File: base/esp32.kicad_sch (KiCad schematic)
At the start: 7 parts, among them SW1 SW_Push_Open, SW2 SW_Push_Open, U2 ESP32-S3-WROOM-2

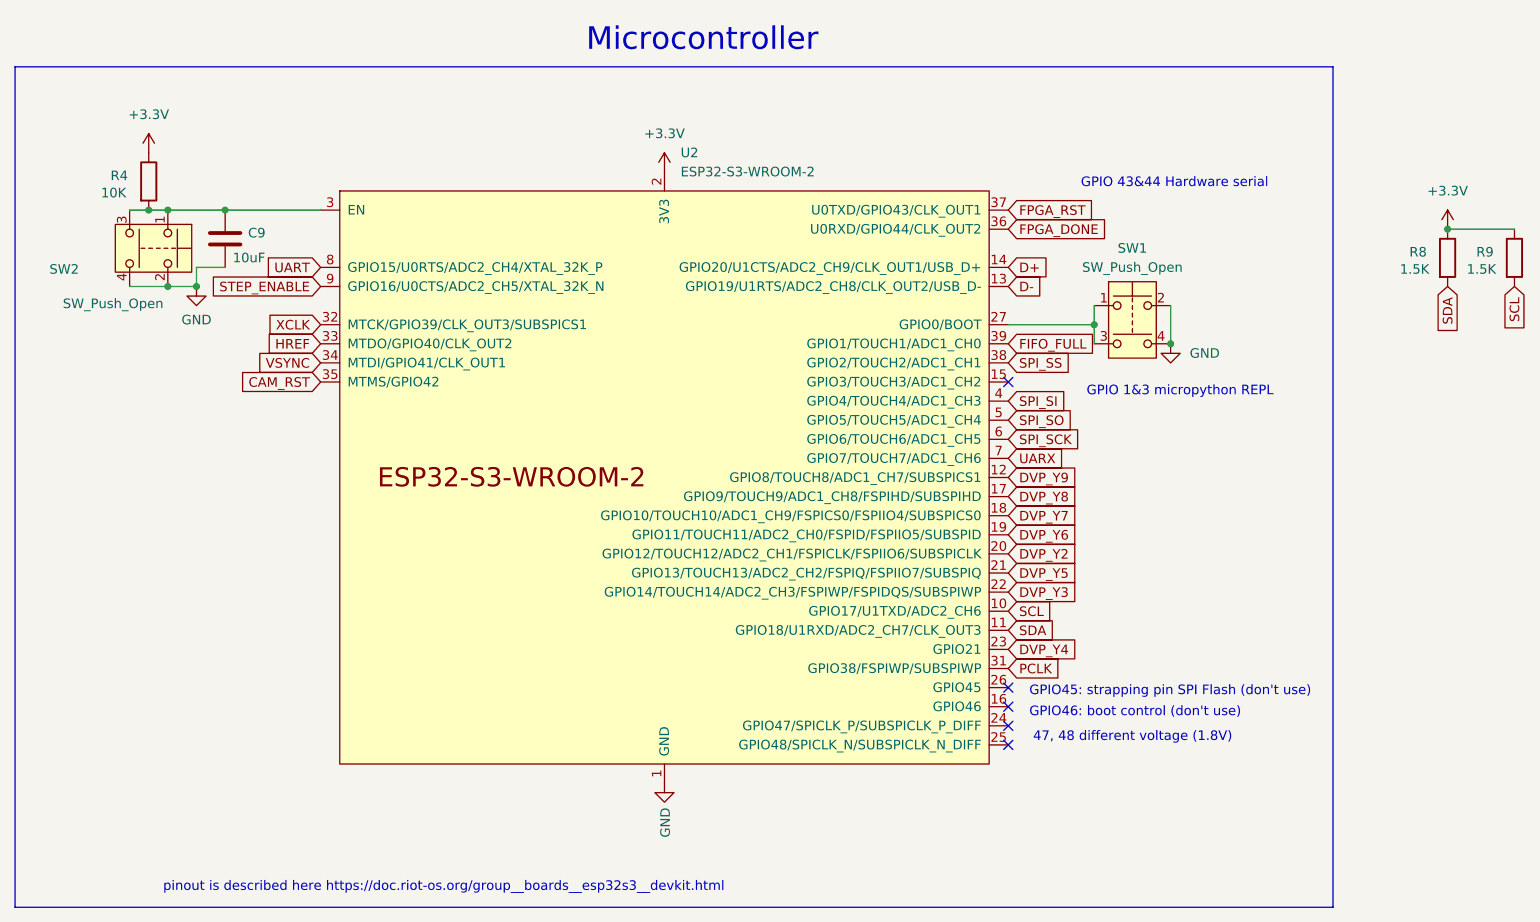
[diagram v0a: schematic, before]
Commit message: improved powernet, fixed bugs, tuned tracks for camera
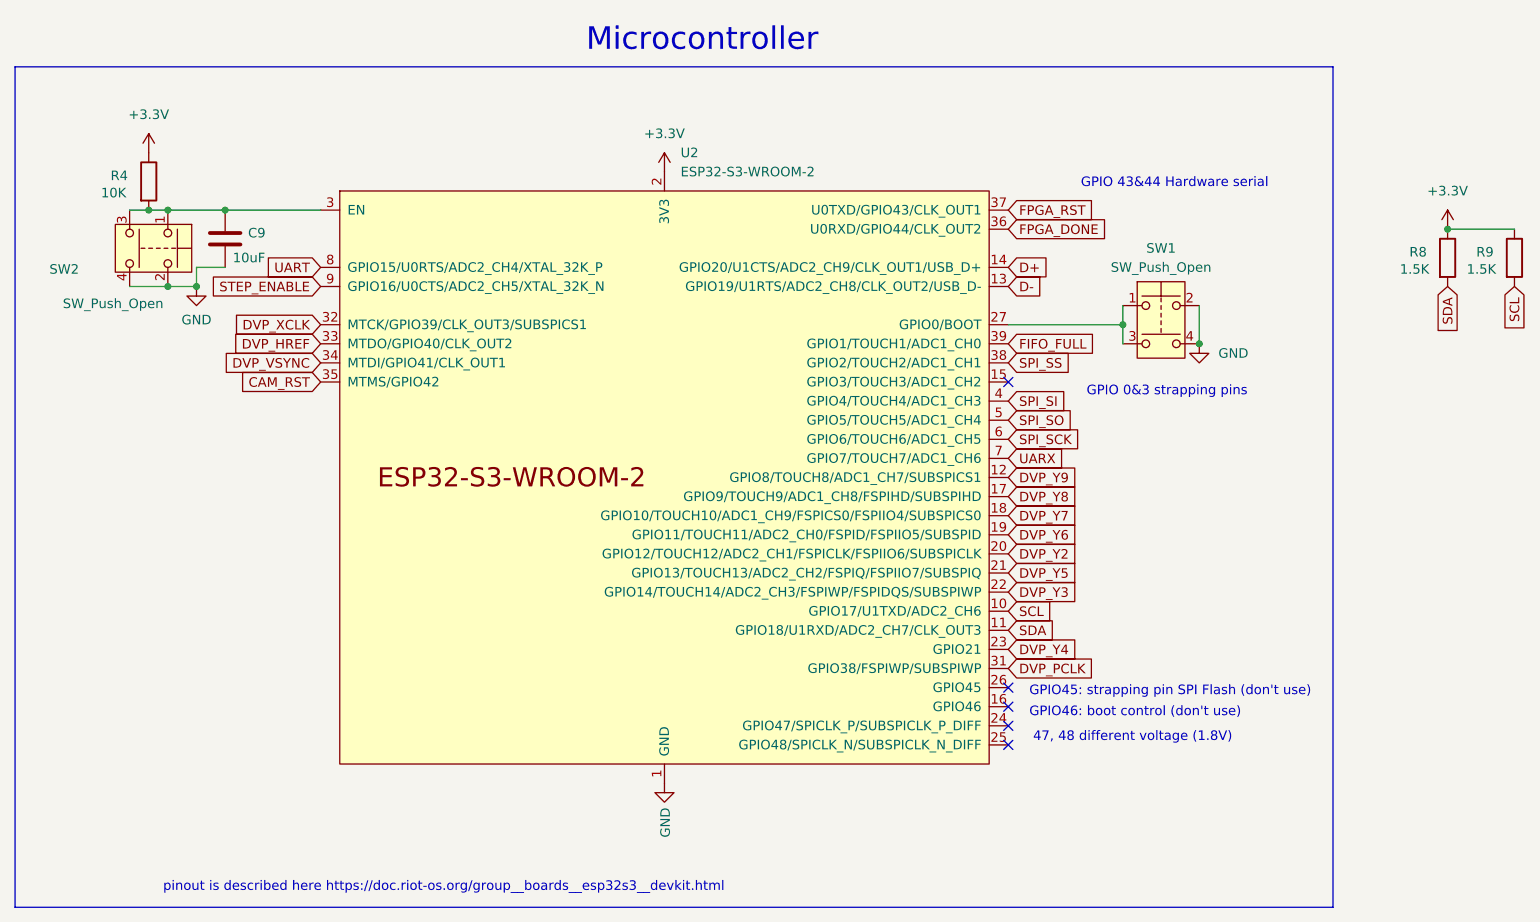
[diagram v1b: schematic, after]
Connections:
- net HREF renamed DVP_HREF
- net PCLK renamed DVP_PCLK
- net VSYNC renamed DVP_VSYNC
- net XCLK renamed DVP_XCLK
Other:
- note added: "GPIO 0&3 strapping pins"
- note removed: "GPIO 1&3 micropython REPL"
- moved on the sheet: SW1
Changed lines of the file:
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@@
 		)
 	)
-	(text "GPIO 1&3 micropython REPL"
+	(text "GPIO 0&3 strapping pins\n"
 		(exclude_from_sim no)
 		(at 190.754 84.582 0)
@@
 	)
 	(junction
-		(at 191.77 74.93)
+		(at 195.58 74.93)
 		(diameter 0)
 		(color 0 0 0 0)
@@
 	)
 	(junction
-		(at 201.93 77.47)
+		(at 205.74 77.47)
 		(diameter 0)
 		(color 0 0 0 0)
@@
 	(wire
 		(pts
-			(xy 191.77 74.93) (xy 191.77 77.47)
+			(xy 76.2 67.31) (xy 72.39 67.31)
 		)
 		(stroke
@@
 	(wire
 		(pts
-			(xy 76.2 67.31) (xy 72.39 67.31)
+			(xy 180.34 74.93) (xy 195.58 74.93)
 		)
 		(stroke
@@
 	(wire
 		(pts
-			(xy 180.34 74.93) (xy 191.77 74.93)
+			(xy 72.39 67.31) (xy 72.39 69.85)
 		)
 		(stroke
@@
 	(wire
 		(pts
-			(xy 72.39 67.31) (xy 72.39 69.85)
+			(xy 205.74 72.39) (xy 205.74 77.47)
 		)
 		(stroke
@@
 	(wire
 		(pts
-			(xy 201.93 72.39) (xy 201.93 77.47)
+			(xy 68.58 69.85) (xy 72.39 69.85)
 		)
 		(stroke
@@
 	(wire
 		(pts
-			(xy 68.58 69.85) (xy 72.39 69.85)
+			(xy 76.2 59.69) (xy 88.9 59.69)
 		)
 		(stroke
@@
 	(wire
 		(pts
-			(xy 76.2 59.69) (xy 88.9 59.69)
+			(xy 66.04 59.69) (xy 68.58 59.69)
 		)
 		(stroke
@@
 	(wire
 		(pts
-			(xy 66.04 59.69) (xy 68.58 59.69)
+			(xy 63.5 59.69) (xy 66.04 59.69)
 		)
 		(stroke
@@
 	(wire
 		(pts
-			(xy 63.5 59.69) (xy 66.04 59.69)
+			(xy 195.58 72.39) (xy 195.58 77.47)
 		)
 		(stroke
@@
 	(wire
 		(pts
-			(xy 191.77 72.39) (xy 191.77 74.93)
+			(xy 238.76 62.23) (xy 247.65 62.23)
 		)
 		(stroke
@@
 	(wire
 		(pts
-			(xy 238.76 62.23) (xy 247.65 62.23)
+			(xy 63.5 69.85) (xy 68.58 69.85)
 		)
 		(stroke
@@
 	(wire
 		(pts
-			(xy 63.5 69.85) (xy 68.58 69.85)
+			(xy 68.58 59.69) (xy 76.2 59.69)
 		)
 		(stroke
@@
 		)
 	)
-	(wire
-		(pts
-			(xy 68.58 59.69) (xy 76.2 59.69)
-		)
-		(stroke
-			(width 0)
-			(type default)
-		)
-	)
-	(global_label "HREF"
+	(global_label "DVP_HREF"
 		(shape input)
 		(at 88.9 77.47 180)
@@
 		)
 		(property "Intersheetrefs" "${INTERSHEET_REFS}"
-			(at 81.7309 77.47 0)
+			(at 77.1347 77.47 0)
 			(hide yes)
 			(show_name no)
@@
 		)
 	)
-	(global_label "VSYNC"
+	(global_label "DVP_VSYNC"
 		(shape input)
 		(at 88.9 80.01 180)
@@
 		)
 		(property "Intersheetrefs" "${INTERSHEET_REFS}"
-			(at 80.5818 80.01 0)
+			(at 75.9856 80.01 0)
 			(hide yes)
 			(show_name no)
@@
 		)
 	)
-	(global_label "XCLK"
+	(global_label "DVP_XCLK"
 		(shape input)
 		(at 88.9 74.93 180)
@@
 		)
 		(property "Intersheetrefs" "${INTERSHEET_REFS}"
-			(at 81.7914 74.93 0)
+			(at 77.1952 74.93 0)
 			(hide yes)
 			(show_name no)
@@
 		)
 	)
-	(global_label "PCLK"
+	(global_label "DVP_PCLK"
 		(shape input)
 		(at 180.34 120.65 0)
@@
 		)
 		(property "Intersheetrefs" "${INTERSHEET_REFS}"
-			(at 187.5091 120.65 0)
+			(at 192.1053 120.65 0)
 			(hide yes)
 			(show_name no)
@@
 	(symbol
 		(lib_id "power:GND")
-		(at 201.93 77.47 0)
+		(at 205.74 77.47 0)
 		(unit 1)
 		(body_style 1)
@@
 		(fields_autoplaced yes)
 		(property "Reference" "#PWR032"
-			(at 201.93 83.82 0)
+			(at 205.74 83.82 0)
 			(hide yes)
 			(show_name no)
@@
 		)
 		(property "Value" "GND"
-			(at 204.47 78.7399 0)
+			(at 208.28 78.7399 0)
 			(show_name no)
 			(do_not_autoplace no)
@@
 		)
 		(property "Footprint" ""
-			(at 201.93 77.47 0)
+			(at 205.74 77.47 0)
 			(hide yes)
 			(show_name no)
@@
 		)
 		(property "Datasheet" ""
-			(at 201.93 77.47 0)
+			(at 205.74 77.47 0)
 			(hide yes)
 			(show_name no)
@@
 		)
 		(property "Description" "Power symbol creates a global label with name \"GND\" , ground"
-			(at 201.93 77.47 0)
+			(at 205.74 77.47 0)
 			(hide yes)
 			(show_name no)
@@
 	(symbol
 		(lib_id "Switch:SW_Push_Dual")
-		(at 196.85 74.93 0)
+		(at 200.66 74.93 0)
 		(unit 1)
 		(body_style 1)
@@
 		(fields_autoplaced yes)
 		(property "Reference" "SW1"
-			(at 196.85 64.77 0)
+			(at 200.66 64.77 0)
 			(show_name no)
 			(do_not_autoplace no)
@@
 		)
 		(property "Value" "SW_Push_Open"
-			(at 196.85 67.31 0)
+			(at 200.66 67.31 0)
 			(show_name no)
 			(do_not_autoplace no)
@@
 		)
 		(property "Footprint" "footprints:SKRPABE010"
-			(at 196.85 67.31 0)
+			(at 200.66 67.31 0)
 			(hide yes)
 			(show_name no)
@@
 		)
 		(property "Datasheet" "https://nl.farnell.com/en-NL/alcoswitch-te-connectivity/fsmsm/switch-spst-0-05a-24vdc-smd/dp/1703878"
-			(at 196.85 74.93 0)
+			(at 200.66 74.93 0)
 			(hide yes)
 			(show_name no)
@@
 		)
 		(property "Description" "Push button switch, generic, symbol, four pins"
-			(at 196.85 74.93 0)
+			(at 200.66 74.93 0)
 			(hide yes)
 			(show_name no)
@@
 		)
 		(property "farnell#" "3261824"
-			(at 196.85 74.93 0)
+			(at 200.66 74.93 0)
 			(hide yes)
 			(show_name no)
@@
 		)
 		(property "manf#" "SKRPABE010"
-			(at 196.85 74.93 0)
+			(at 200.66 74.93 0)
 			(hide yes)
 			(show_name no)
@@
 		)
 		(property "mouser#" "688-SKRPAB"
-			(at 196.85 74.93 0)
+			(at 200.66 74.93 0)
 			(hide yes)
 			(show_name no)
@@
 		)
 		(property "OLDFootprint" ""
-			(at 196.85 74.93 0)
-			(hide yes)
-			(show_name no)
+			(at 200.66 74.93 0)
+			(hide yes)
+			(show_name no)

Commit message: send to fab
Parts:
- R4: value 10K -> 5.1K; farnell# 2826162 -> 1469937; manf# CRCW080510K0JNEAC -> CRCW08055K10FKEA; mouser# 71-CRCW080510K0JNEAC -> -71-CRCW0805-5.1K-E3
- R8, R9: value 1.5K -> 5.1K; farnell# 2908429 -> 1469937; manf# CR0805-JW-152ELF -> CRCW08055K10FKEA; mouser# 652-CR0805JW-152ELF -> -71-CRCW0805-5.1K-E3
- SW1, SW2: mouser# 688-SKRPAB -> 611-PTS810SJM250SMTR
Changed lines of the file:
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@@
 			)
 		)
-		(property "Value" "1.5K"
+		(property "Value" "5.1K"
 			(at 232.41 67.564 0)
 			(show_name no)
@@
 			)
 		)
-		(property "farnell#" "2908429"
+		(property "farnell#" "1469937"
 			(at 238.76 66.04 0)
 			(hide yes)
@@
 			)
 		)
-		(property "manf#" "CR0805-JW-152ELF"
+		(property "manf#" "CRCW08055K10FKEA"
 			(at 238.76 66.04 0)
 			(hide yes)
@@
 			)
 		)
-		(property "mouser#" "652-CR0805JW-152ELF"
+		(property "mouser#" "-71-CRCW0805-5.1K-E3"
 			(at 238.76 66.04 0)
 			(hide yes)
@@
 			)
 		)
-		(property "mouser#" "688-SKRPAB"
+		(property "mouser#" "611-PTS810SJM250SMTR"
 			(at 200.66 74.93 0)
 			(hide yes)
@@
 			)
 		)
-		(property "mouser#" "688-SKRPAB"
+		(property "mouser#" "611-PTS810SJM250SMTR"
 			(at 66.04 64.77 0)
 			(hide yes)
@@
 			)
 		)
-		(property "Value" "1.5K"
+		(property "Value" "5.1K"
 			(at 241.3 67.564 0)
 			(show_name no)
@@
 			)
 		)
-		(property "farnell#" "2908429"
+		(property "farnell#" "1469937"
 			(at 247.65 66.04 0)
 			(hide yes)
@@
 			)
 		)
-		(property "manf#" "CR0805-JW-152ELF"
+		(property "manf#" "CRCW08055K10FKEA"
 			(at 247.65 66.04 0)
 			(hide yes)
@@
 			)
 		)
-		(property "mouser#" "652-CR0805JW-152ELF"
+		(property "mouser#" "-71-CRCW0805-5.1K-E3"
 			(at 247.65 66.04 0)
 			(hide yes)
@@
 			)
 		)
-		(property "Value" "10K"
+		(property "Value" "5.1K"
 			(at 59.69 57.404 0)
 			(show_name no)
@@
 			)
 		)
-		(property "farnell#" "2826162"
+		(property "farnell#" "1469937"
 			(at 66.04 55.88 0)
 			(hide yes)
@@
 			)
 		)
-		(property "manf#" "CRCW080510K0JNEAC"
+		(property "manf#" "CRCW08055K10FKEA"
 			(at 66.04 55.88 0)
 			(hide yes)
@@
 			)
 		)
-		(property "mouser#" "71-CRCW080510K0JNEAC"
+		(property "mouser#" "-71-CRCW0805-5.1K-E3"
 			(at 66.04 55.88 0)
 			(hide yes)

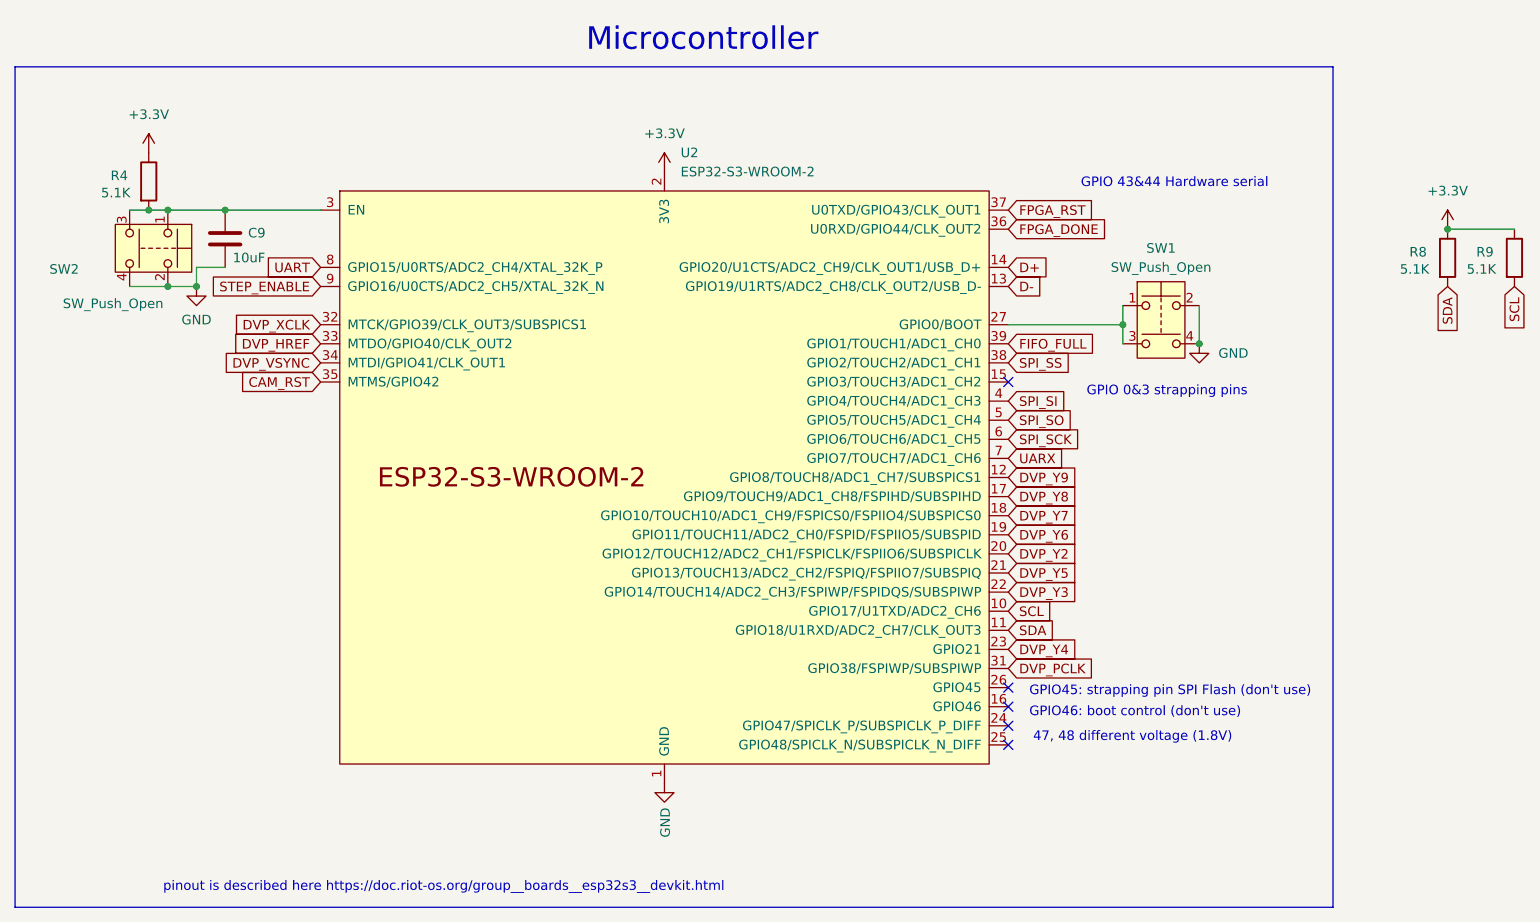
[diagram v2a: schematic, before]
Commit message: fixed: uartx res to 5.1K, switch connection cross, camera connextor top side
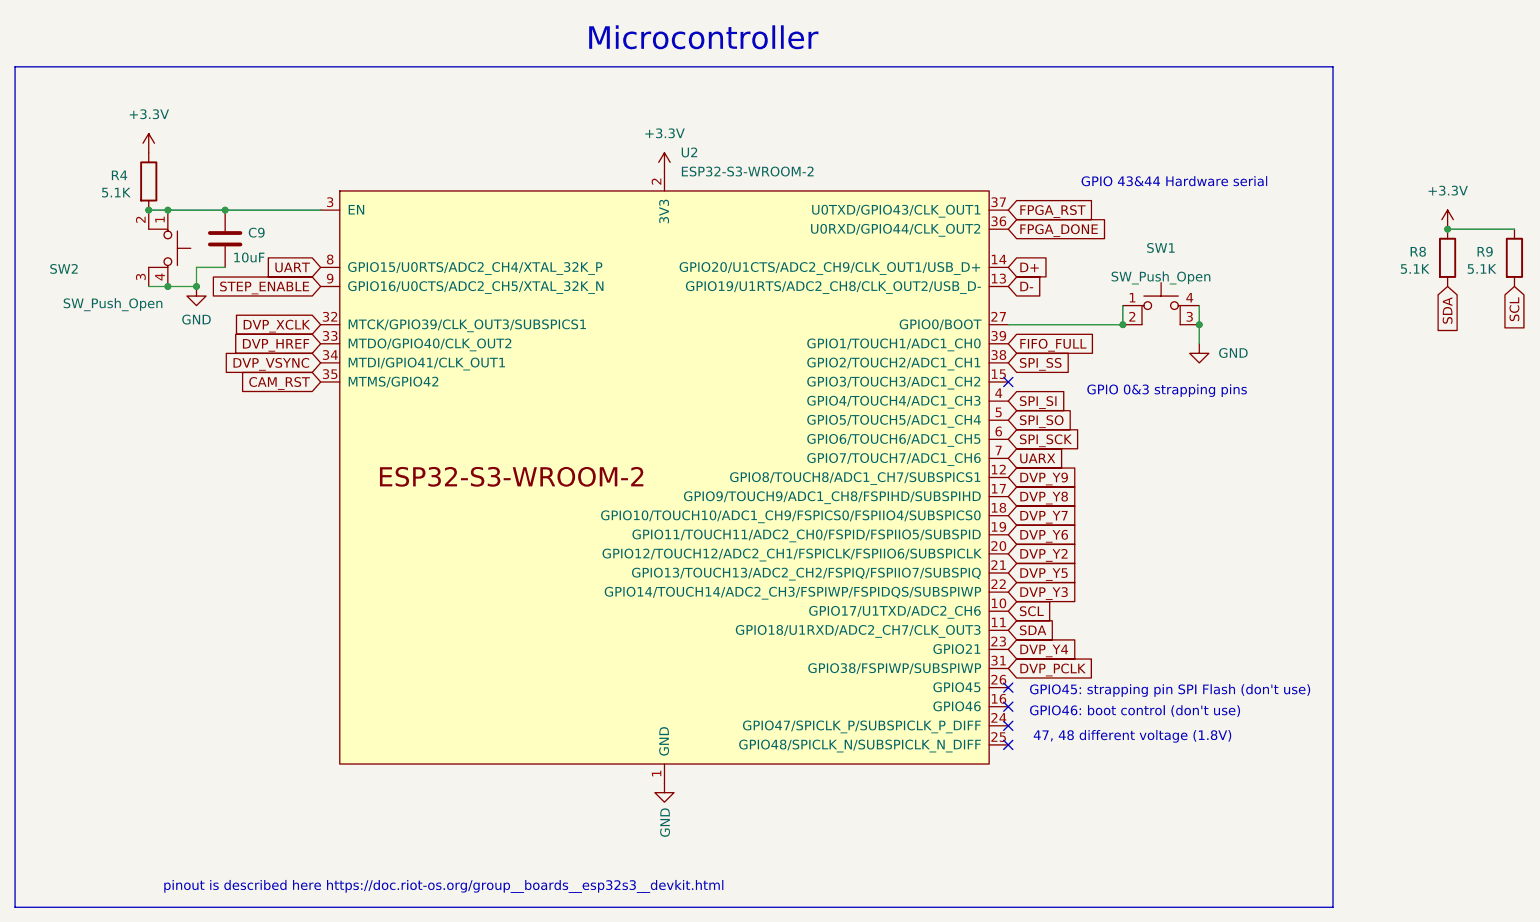
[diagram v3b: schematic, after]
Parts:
- SW1, SW2: symbol Switch:SW_Push_Dual -> Switch:SW_MEC_5E
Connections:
- net GND: now also SW1.3 (K), SW2.3 (K); no longer SW1.2, SW2.2
- net at SW1.1, U2.27 (GPIO0/BOOT): now also SW1.2; no longer SW1.3
- net at C9.1, R4.2, SW2.1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: now also SW2.2; no longer SW2.3
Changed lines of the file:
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@@
+	)
+	(junction
+		(at 68.58 69.85)
+		(diameter 0)
+		(color 0 0 0 0)
 	)
 	(junction
@@
 	)
 	(junction
-		(at 205.74 77.47)
-		(diameter 0)
-		(color 0 0 0 0)
-	)
-	(junction
-		(at 68.58 69.85)
+		(at 205.74 74.93)
 		(diameter 0)
 		(color 0 0 0 0)
@@
 	(wire
 		(pts
-			(xy 180.34 74.93) (xy 195.58 74.93)
+			(xy 205.74 74.93) (xy 205.74 77.47)
 		)
 		(stroke
@@
 	(wire
 		(pts
-			(xy 72.39 67.31) (xy 72.39 69.85)
+			(xy 180.34 74.93) (xy 195.58 74.93)
 		)
 		(stroke
@@
 	(wire
 		(pts
-			(xy 205.74 72.39) (xy 205.74 77.47)
+			(xy 72.39 67.31) (xy 72.39 69.85)
 		)
 		(stroke
@@
 	(wire
 		(pts
-			(xy 68.58 69.85) (xy 72.39 69.85)
+			(xy 205.74 72.39) (xy 205.74 74.93)
 		)
 		(stroke
@@
 	(wire
 		(pts
-			(xy 76.2 59.69) (xy 88.9 59.69)
+			(xy 68.58 69.85) (xy 72.39 69.85)
 		)
 		(stroke
@@
 	(wire
 		(pts
-			(xy 66.04 59.69) (xy 68.58 59.69)
+			(xy 76.2 59.69) (xy 88.9 59.69)
 		)
 		(stroke
@@
 	(wire
 		(pts
-			(xy 63.5 59.69) (xy 66.04 59.69)
+			(xy 66.04 69.85) (xy 68.58 69.85)
 		)
 		(stroke
@@
 	(wire
 		(pts
-			(xy 195.58 72.39) (xy 195.58 77.47)
+			(xy 66.04 59.69) (xy 68.58 59.69)
 		)
 		(stroke
@@
 	(wire
 		(pts
-			(xy 238.76 62.23) (xy 247.65 62.23)
+			(xy 195.58 72.39) (xy 195.58 74.93)
 		)
 		(stroke
@@
 	(wire
 		(pts
-			(xy 63.5 69.85) (xy 68.58 69.85)
+			(xy 238.76 62.23) (xy 247.65 62.23)
 		)
 		(stroke
@@
 	)
 	(symbol
-		(lib_id "Switch:SW_Push_Dual")
+		(lib_id "Switch:SW_MEC_5E")
 		(at 200.66 74.93 0)
 		(unit 1)
@@
 		(in_pos_files yes)
 		(dnp no)
-		(fields_autoplaced yes)
 		(property "Reference" "SW1"
 			(at 200.66 64.77 0)
@@
 		)
 		(property "Value" "SW_Push_Open"
-			(at 200.66 67.31 0)
+			(at 200.66 68.58 0)
 			(show_name no)
 			(do_not_autoplace no)
@@
 			)
 		)
-		(property "Datasheet" "https://nl.farnell.com/en-NL/alcoswitch-te-connectivity/fsmsm/switch-spst-0-05a-24vdc-smd/dp/1703878"
-			(at 200.66 74.93 0)
-			(hide yes)
-			(show_name no)
-			(do_not_autoplace no)
-			(effects
-				(font
-					(size 1.27 1.27)
-				)
-			)
-		)
-		(property "Description" "Push button switch, generic, symbol, four pins"
+		(property "Datasheet" "https://www.apem.com/medias/download/MEC_switches_serie_MULTIMEC5E.pdf"
+			(at 200.66 67.31 0)
+			(hide yes)
+			(show_name no)
+			(do_not_autoplace no)
+			(effects
+				(font
+					(size 1.27 1.27)
+				)
+			)
+		)
+		(property "Description" "MEC 5E single pole normally-open tactile switch"
 			(at 200.66 74.93 0)
 			(hide yes)
@@
 	)
 	(symbol
-		(lib_id "Switch:SW_Push_Dual")
+		(lib_id "Switch:SW_MEC_5E")
 		(at 66.04 64.77 270)
 		(unit 1)
@@
 			)
 		)
-		(property "Datasheet" "https://nl.farnell.com/en-NL/alcoswitch-te-connectivity/fsmsm/switch-spst-0-05a-24vdc-smd/dp/1703878"
+		(property "Datasheet" "https://www.apem.com/medias/download/MEC_switches_serie_MULTIMEC5E.pdf"
+			(at 73.66 64.77 0)
+			(hide yes)
+			(show_name no)
+			(do_not_autoplace no)
+			(effects
+				(font
+					(size 1.27 1.27)
+				)
+			)
+		)
+		(property "Description" "MEC 5E single pole normally-open tactile switch"
 			(at 66.04 64.77 0)
 			(hide yes)
-			(show_name no)
-			(do_not_autoplace no)
-			(effects
-				(font
-					(size 1.27 1.27)
-				)
-			)
-		)
-		(property "Description" "Push button switch, generic, symbol, four pins"
-			(at 66.04 64.77 0)
-			(hide yes)
